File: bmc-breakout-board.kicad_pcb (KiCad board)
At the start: 4 copper layers, 90 x 60 mm, 42 parts, among them J1 PinHeader_2x4, J10 PinHeader_2x4, J11 PinHeader_2x05, J12 61300411121, J13 0473460001, J14 PCIE_BUS_x1, J15 0473460001, J16 PinHeader_1x07, J17 UE27AC54100, J2 PinHeader_2x13, J3 PinHeader_2x08, J4 61300411121, J5 ME1016813401101, J6 61300411121, J7 DC_SOCKET, J8 PinHeader_2x05, J9 PinHeader_1x07, Q1 BSS138AKA, U1 FT234XD-R

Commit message: Update component arrangement
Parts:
- added C10: C_10u_25V_0603, bmc-breakout-board-footprints:0603-cap, F.Cu at (62.8, 99.7)
- added C11: C_100n_0402_16V, bmc-breakout-board-footprints:0402-cap, F.Cu at (63.0, 98.3)
- added C12: C_1n_0603, bmc-breakout-board-footprints:0603-cap, F.Cu at (62.8, 101.3)
- added C8: C_1n_0603, bmc-breakout-board-footprints:0603-cap, F.Cu at (66.4, 107.1)
- added C9: C_100n_0402_16V, bmc-breakout-board-footprints:0402-cap, F.Cu at (67.8, 107.4)
- added L1: 744235900, antmicro-footprints:744235900, F.Cu at (62.9, 106.1)
- added N2: oshw_logo, antmicro-footprints:oshw-logo, F.Cu at (134.0, 72.1)
- Q1: value BSS138AKA -> SI2337DS; footprint bmc-breakout-board-footprints:SOT-23-3 -> antmicro-footprints:SOT-23-3
- S1: value JS202011SCQN -> EG1218; footprint bmc-breakout-board-footprints:Switch_Slide_JS202011SCQN -> antmicro-footprints:Switch_Slide_11.6x4mm_EG1218
- moved R2 13.2 mm to (65.2, 98.3), turned to 0 degrees
- moved Q1 7.81 mm to (66.8, 100.9)
- moved J1 5.22 mm to (71.1, 104.1)
- moved S1 2.17 mm to (63.9, 118.4)
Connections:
- J7 pad 1: P12V_IN -> Net-(C8-Pad1)
- J7 pad 2: GND -> Net-(C8-Pad2)
- J7 pad 3: GND -> Net-(C8-Pad2)
- Q1 pad 2: P12V_AUX -> P12V_IN
- Q1 pad 3: P12V_IN -> P12V_AUX
- R2 pad 2: Net-(R2-Pad2) -> Net-(Q1-Pad1)
- S1 pad 1: GND -> Net-(S1-Pad1)
- S1 pad 3: Net-(R2-Pad2) -> GND
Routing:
- net Net-(R2-Pad2): track 8.31 -> 0.00 mm
- net I3C[0]_SCL: track 42.7 -> 39.0 mm
- net Net-(Q1-Pad1): track 17.5 -> 21.2 mm, vias 0 -> 1
- net I3C[0]_SDA: track 45.4 -> 41.7 mm
- net I3C[1]_SCL: track 41.4 -> 38.4 mm
- net I3C[1]_SDA: track 44.1 -> 41.2 mm
- net I3C[2]_SCL: track 40.0 -> 37.8 mm
- net I3C[2]_SDA: track 42.8 -> 40.6 mm
- net I3C[3]_SCL: track 39.2 -> 37.3 mm
- net P12V_IN: track 2.77 -> 1.23 mm
- net UART0_SCM_TX: track 76.2 -> 77.5 mm
- net I3C[3]_SDA: track 41.4 -> 40.1 mm
- net UART0_SCM_RX: track 73.1 -> 74.3 mm
- net P12V_AUX: vias 15 -> 10
- net GND: vias 35 -> 31
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- added copper zone on F.Cu, net Net-(C8-Pad1)
- added copper zone on F.Cu, net Net-(C8-Pad2)
- removed copper zone on B.Cu, net P12V_AUX

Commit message: Layout updates
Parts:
- moved J6 3.46 mm to (76.0, 83.1)
- moved J8 1.16 mm to (88.1, 83.1)
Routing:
- net I2C[0]_SCL: track 52.7 -> 14.1 mm
- net I2C[2]_SCL: track 50.5 -> 16.7 mm, vias 0 -> 1
- net I2C[3]_SDA: track 46.5 -> 12.8 mm, vias 0 -> 1
- net I2C[3]_SCL: track 49.3 -> 16.2 mm, vias 0 -> 1
- net I2C[1]_SCL: track 52.9 -> 20.6 mm, vias 0 -> 1
- net I2C[1]_SDA: track 49.0 -> 16.8 mm, vias 0 -> 1
- net I2C[2]_SDA: track 46.9 -> 14.8 mm, vias 0 -> 1
- net I2C[4]_SDA: track 46.9 -> 14.9 mm, vias 0 -> 1
- net I2C[0]_SDA: track 49.2 -> 17.7 mm, vias 0 -> 1
- net VIRTUAL_RESEAT: track 91.3 -> 63.1 mm, vias 2 -> 3
- net I2C[4]_SCL: track 49.7 -> 24.9 mm, vias 0 -> 1
- net PCIE_BMC_CLK_100_N: track 71.1 -> 59.4 mm, vias 2 -> 1
- net PCIE_BMC_CLK_100_P: track 70.6 -> 59.3 mm, vias 2 -> 1
- net /TX_N: track 61.2 -> 51.2 mm, vias 1 -> 0
- net /RX_N: track 60.2 -> 51.1 mm, vias 1 -> 0
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
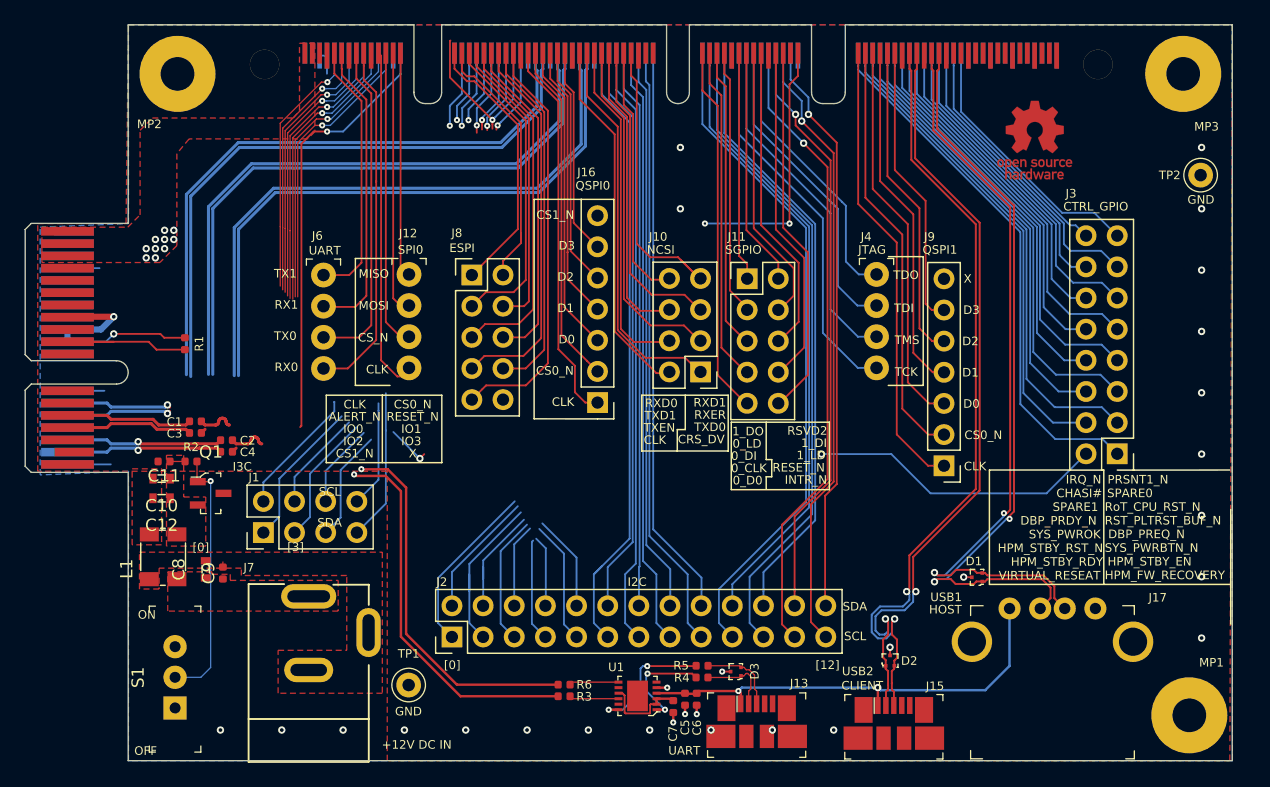
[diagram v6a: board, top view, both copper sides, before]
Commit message: Route unconnected nets, update PCIe
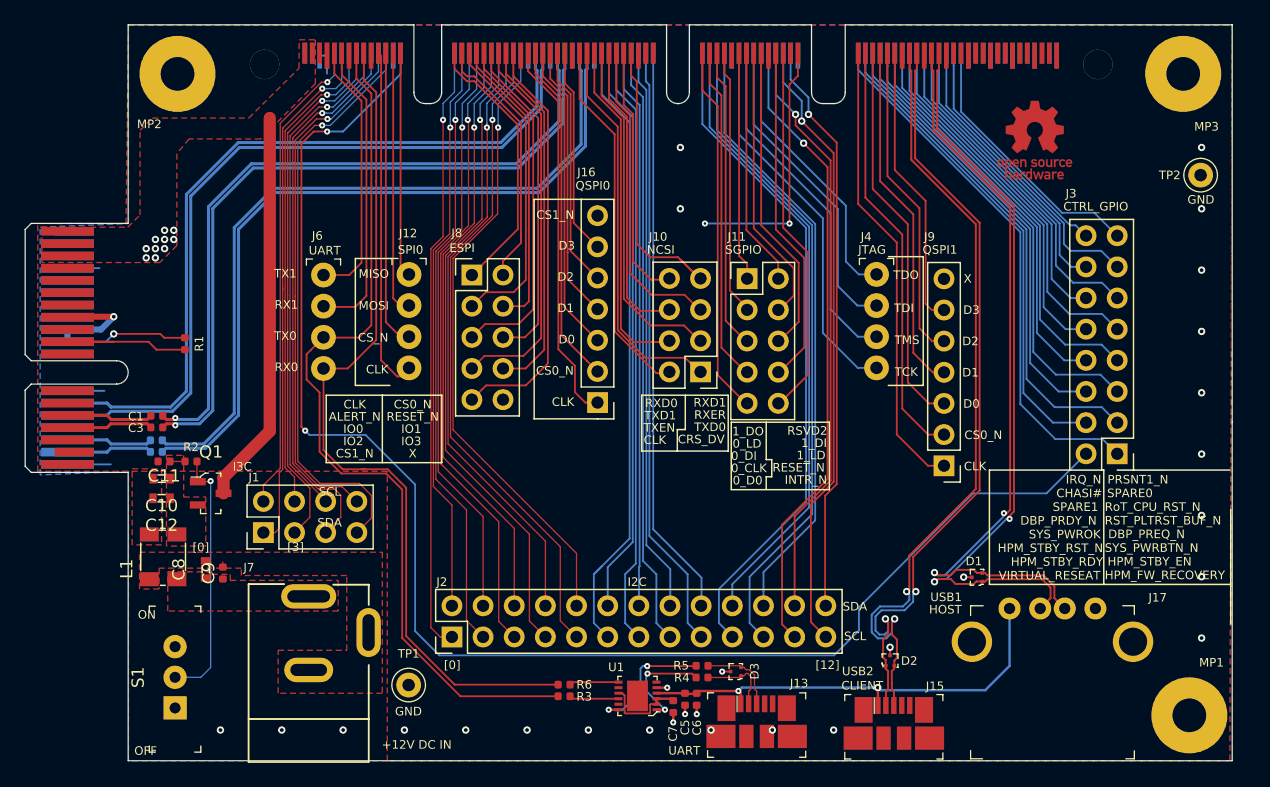
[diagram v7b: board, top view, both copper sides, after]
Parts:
- C2, C4: moved to B.Cu
- moved C2 5.72 mm to (62.4, 96.5)
- moved C4 5.72 mm to (62.4, 97.5)
- moved C1 3.18 mm to (62.4, 94.5)
- moved C3 3.18 mm to (62.4, 95.5)
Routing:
- net VIRTUAL_RESEAT: track 63.1 -> 121.8 mm, vias 3 -> 2
- net I2C[3]_SDA: track 12.8 -> 50.5 mm
- net I2C[4]_SDA: track 14.9 -> 51.8 mm
- net I2C[3]_SCL: track 16.2 -> 52.8 mm
- net I2C[0]_SCL: track 14.1 -> 49.7 mm, vias 0 -> 1
- net I2C[2]_SCL: track 16.7 -> 51.5 mm
- net I2C[2]_SDA: track 14.8 -> 49.1 mm
- net P12V_AUX: track 0.00 -> 32.2 mm
- net I2C[1]_SDA: track 16.8 -> 48.0 mm
- net I2C[1]_SCL: track 20.6 -> 50.3 mm
- net I2C[4]_SCL: track 24.9 -> 54.0 mm
- net I2C[0]_SDA: track 17.7 -> 46.8 mm
- net UART0_SCM_TX: track 73.1 -> 87.1 mm, vias 1 -> 0
- net I3C[2]_SDA: track 32.5 -> 45.4 mm
- net I3C[3]_SDA: track 35.9 -> 47.7 mm
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
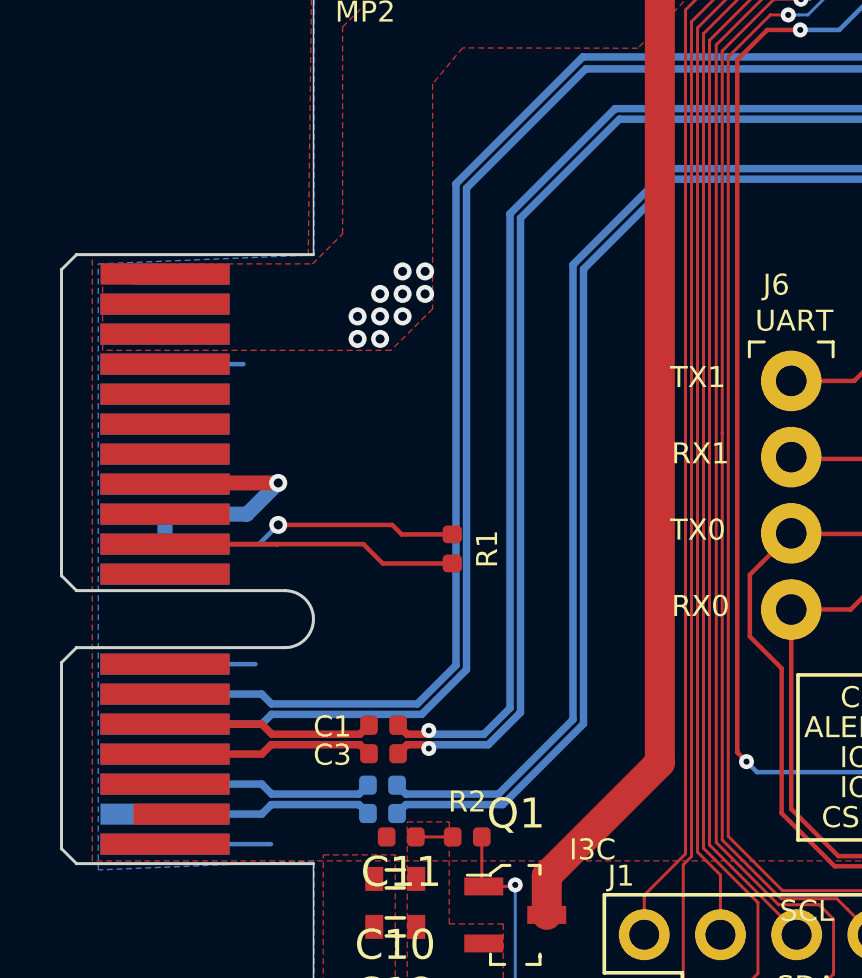
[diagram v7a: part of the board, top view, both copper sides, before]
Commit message: PCIe length matched
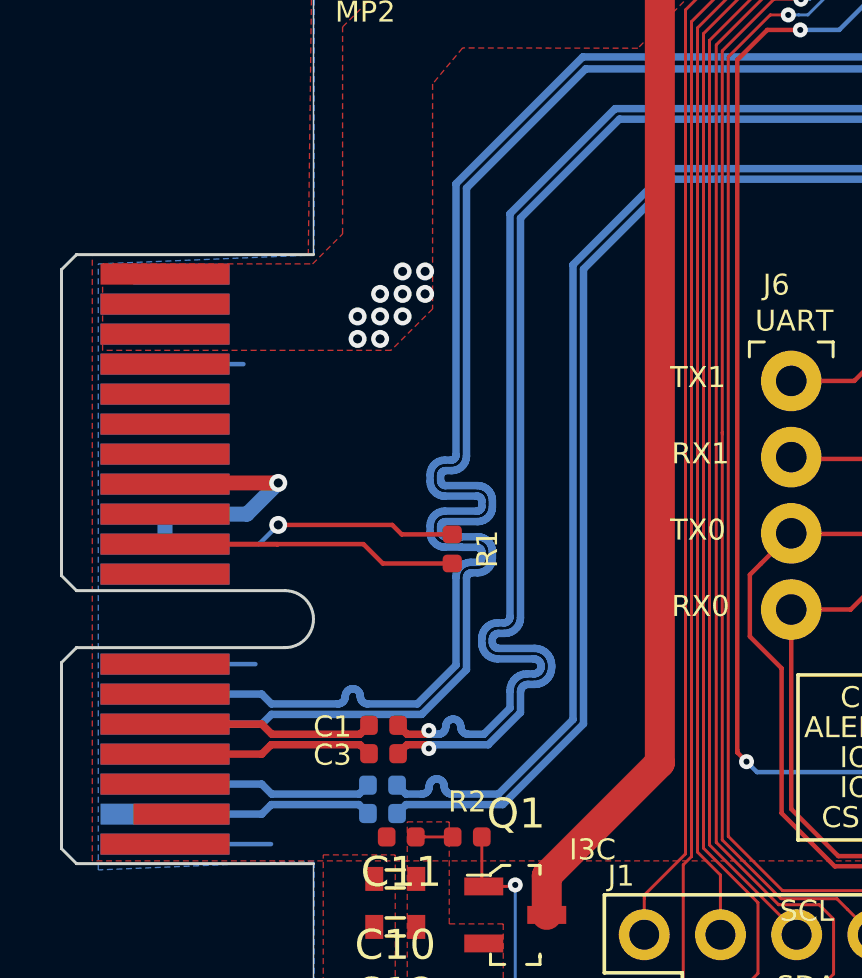
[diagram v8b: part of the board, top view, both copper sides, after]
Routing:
- net PCIE_BMC_CLK_100_P: track 62.4 -> 68.4 mm
- net PCIE_BMC_CLK_100_N: track 62.9 -> 68.4 mm
- net /TX_P: track 57.9 -> 61.4 mm
- net /TX_N: track 58.4 -> 61.4 mm
- net /RX_P: track 60.8 -> 61.3 mm
